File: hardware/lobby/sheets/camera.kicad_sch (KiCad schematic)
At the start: 1 part

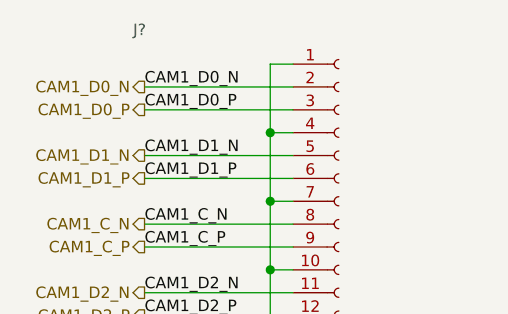
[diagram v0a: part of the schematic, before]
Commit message: start routing mezzanine
making a progress capture before trying to cram a lot of signals onto just one hirose connector...
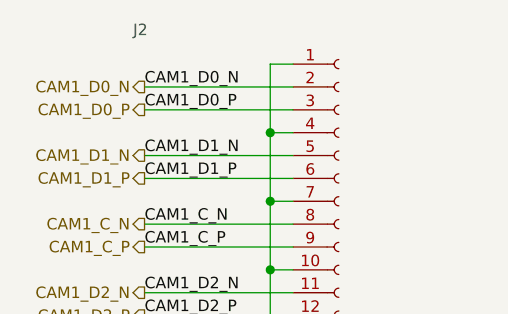
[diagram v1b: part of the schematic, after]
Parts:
- gave numbers to parts that had none: 1
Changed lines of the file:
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@@
   (symbol (lib_id "power:GND") (at 146.05 113.03 0) (unit 1)
     (in_bom yes) (on_board yes)
-    (property "Reference" "#PWR?" (id 0) (at 146.05 119.38 0)
+    (property "Reference" "#PWR0117" (id 0) (at 146.05 119.38 0)
       (effects (font (size 1.27 1.27)) hide)
     )
@@
   (symbol (lib_id "Connector:Conn_01x22_Female") (at 153.67 83.82 0) (unit 1)
     (in_bom yes) (on_board yes)
-    (property "Reference" "J?" (id 0) (at 130.81 54.61 0)
+    (property "Reference" "J2" (id 0) (at 130.81 54.61 0)
       (effects (font (size 1.27 1.27)) (justify left))
     )

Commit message: sheet refs relative, copied escalator pinout to lobby
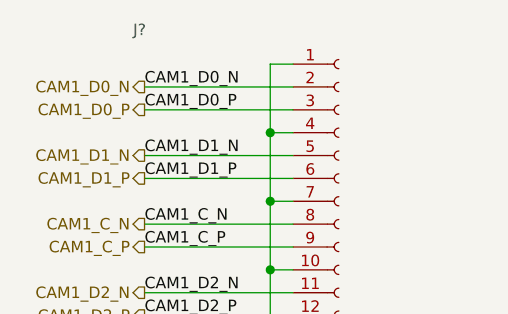
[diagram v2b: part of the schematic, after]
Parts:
- renumbered J2 to J?
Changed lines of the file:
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@@
   (symbol (lib_id "power:GND") (at 146.05 113.03 0) (unit 1)
     (in_bom yes) (on_board yes)
-    (property "Reference" "#PWR0117" (id 0) (at 146.05 119.38 0)
+    (property "Reference" "#PWR?" (id 0) (at 146.05 119.38 0)
       (effects (font (size 1.27 1.27)) hide)
     )
@@
   (symbol (lib_id "Connector:Conn_01x22_Female") (at 153.67 83.82 0) (unit 1)
     (in_bom yes) (on_board yes)
-    (property "Reference" "J2" (id 0) (at 130.81 54.61 0)
+    (property "Reference" "J?" (id 0) (at 130.81 54.61 0)
       (effects (font (size 1.27 1.27)) (justify left))
     )

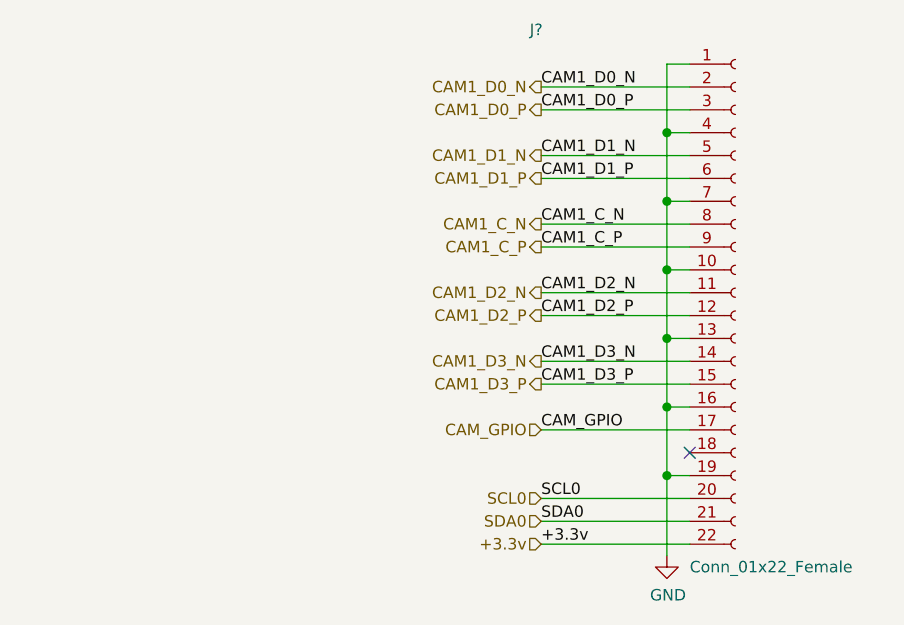
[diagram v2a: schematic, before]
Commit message: work abroad
did some light planning for the lobby board while on vacation. now ready for final placement + routing
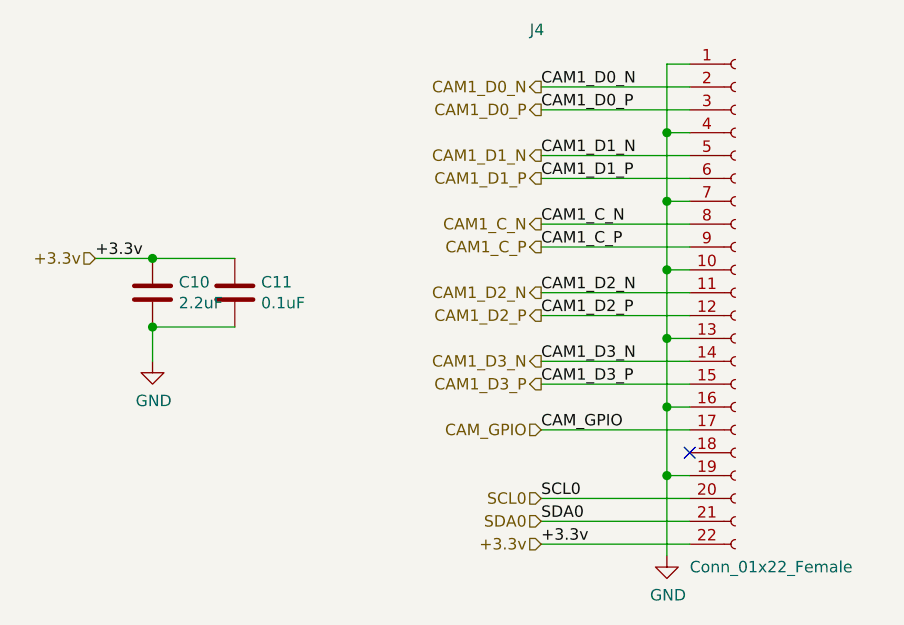
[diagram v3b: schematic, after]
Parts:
- added C10: 2.2uF, Capacitor_SMD:C_0603_1608Metric, symbol Device:C
- added C11: 0.1uF, Capacitor_SMD:C_0603_1608Metric, symbol Device:C
- gave numbers to parts that had none: 1
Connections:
- net +3.3v: now also C10.1, C11.1
- net GND: now also C10.2, C11.2
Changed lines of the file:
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@@
 (kicad_sch (version 20210406) (generator eeschema)
   (paper "A4")
+  (junction (at 88.9 80.01) (diameter 1.016) (color 0 0 0 0))
+  (junction (at 88.9 87.63) (diameter 1.016) (color 0 0 0 0))
   (junction (at 146.05 66.04) (diameter 1.016) (color 0 0 0 0))
   (junction (at 146.05 73.66) (diameter 1.016) (color 0 0 0 0))
@@
   (junction (at 146.05 104.14) (diameter 1.016) (color 0 0 0 0))
   (no_connect (at 148.59 101.6))
+  (wire (pts (xy 82.55 80.01) (xy 88.9 80.01))
+    (stroke (width 0) (type solid) (color 0 0 0 0))
+  )
+  (wire (pts (xy 88.9 80.01) (xy 98.044 80.01))
+    (stroke (width 0) (type solid) (color 0 0 0 0))
+  )
+  (wire (pts (xy 88.9 87.63) (xy 98.044 87.63))
+    (stroke (width 0) (type solid) (color 0 0 0 0))
+  )
+  (wire (pts (xy 88.9 91.44) (xy 88.9 87.63))
+    (stroke (width 0) (type solid) (color 0 0 0 0))
+  )
   (wire (pts (xy 132.08 60.96) (xy 148.59 60.96))
     (stroke (width 0) (type solid) (color 0 0 0 0))
@@
     (stroke (width 0) (type solid) (color 0 0 0 0))
   )
+  (label "+3.3v" (at 82.55 80.01 0)
+    (effects (font (size 1.27 1.27)) (justify left bottom))
+  )
   (label "CAM1_D0_N" (at 132.08 60.96 0)
     (effects (font (size 1.27 1.27)) (justify left bottom))
@@
     (effects (font (size 1.27 1.27)) (justify left bottom))
   )
+  (hierarchical_label "+3.3v" (shape input) (at 82.55 80.01 180)
+    (effects (font (size 1.27 1.27)) (justify right))
+  )
   (hierarchical_label "CAM1_D0_N" (shape output) (at 132.08 60.96 180)
     (effects (font (size 1.27 1.27)) (justify right))
@@
     (effects (font (size 1.27 1.27)) (justify right))
   )
+  (symbol (lib_id "power:GND") (at 88.9 91.44 0) (unit 1)
+    (in_bom yes) (on_board yes)
+    (property "Reference" "#PWR0101" (id 0) (at 88.9 97.79 0)
+      (effects (font (size 1.27 1.27)) hide)
+    )
+    (property "Value" "GND" (id 1) (at 89.027 95.8342 0))
+    (property "Footprint" "" (id 2) (at 88.9 91.44 0)
+      (effects (font (size 1.27 1.27)) hide)
+    )
+    (property "Datasheet" "" (id 3) (at 88.9 91.44 0)
+      (effects (font (size 1.27 1.27)) hide)
+    )
+    (pin "1")
+  )
   (symbol (lib_id "power:GND") (at 146.05 113.03 0) (unit 1)
     (in_bom yes) (on_board yes)
-    (property "Reference" "#PWR?" (id 0) (at 146.05 119.38 0)
+    (property "Reference" "#PWR0102" (id 0) (at 146.05 119.38 0)
       (effects (font (size 1.27 1.27)) hide)
     )
@@
     (pin "1")
   )
+  (symbol (lib_id "Device:C") (at 88.9 83.82 0) (unit 1)
+    (in_bom yes) (on_board yes)
+    (property "Reference" "C10" (id 0) (at 91.821 82.6516 0)
+      (effects (font (size 1.27 1.27)) (justify left))
+    )
+    (property "Value" "2.2uF" (id 1) (at 91.821 84.963 0)
+      (effects (font (size 1.27 1.27)) (justify left))
+    )
+    (property "Footprint" "Capacitor_SMD:C_0603_1608Metric" (id 2) (at 89.8652 87.63 0)
+      (effects (font (size 1.27 1.27)) hide)
+    )
+    (property "Datasheet" "https://search.murata.co.jp/Ceramy/image/img/A01X/G101/ENG/GRM21BR71A106KA73-01.pdf" (id 3) (at 88.9 83.82 0)
+      (effects (font (size 1.27 1.27)) hide)
+    )
+    (property "Field5" "490-14381-1-ND" (id 4) (at 88.9 83.82 0)
+      (effects (font (size 1.27 1.27)) hide)
+    )
+    (property "Field4" "Digikey" (id 5) (at 88.9 83.82 0)
+      (effects (font (size 1.27 1.27)) hide)
+    )
+    (property "Field6" "GRM21BR71A106KA73L" (id 6) (at 88.9 83.82 0)
+      (effects (font (size 1.27 1.27)) hide)
+    )
+    (property "Field7" "Murata" (id 7) (at 88.9 83.82 0)
+      (effects (font (size 1.27 1.27)) hide)
+    )
+    (property "Part Description" "	10uF 10% 10V Ceramic Capacitor X7R 0805 (2012 Metric)" (id 8) (at 88.9 83.82 0)
+      (effects (font (size 1.27 1.27)) hide)
+    )
+    (property "Field8" "111893011" (id 9) (at 88.9 83.82 0)
+      (effects (font (size 1.27 1.27)) hide)
+    )
+    (pin "1")
+    (pin "2")
+  )
+  (symbol (lib_id "Device:C") (at 98.044 83.82 0) (unit 1)
+    (in_bom yes) (on_board yes)
+    (property "Reference" "C11" (id 0) (at 100.965 82.6516 0)
+      (effects (font (size 1.27 1.27)) (justify left))
+    )
+    (property "Value" "0.1uF" (id 1) (at 100.965 84.963 0)
+      (effects (font (size 1.27 1.27)) (justify left))
+    )
+    (property "Footprint" "Capacitor_SMD:C_0603_1608Metric" (id 2) (at 99.0092 87.63 0)
+      (effects (font (size 1.27 1.27)) hide)
+    )
+    (property "Datasheet" "https://search.murata.co.jp/Ceramy/image/img/A01X/G101/ENG/GRM21BR71A106KA73-01.pdf" (id 3) (at 98.044 83.82 0)
+      (effects (font (size 1.27 1.27)) hide)
+    )
+    (property "Field5" "490-14381-1-ND" (id 4) (at 98.044 83.82 0)
+      (effects (font (size 1.27 1.27)) hide)
+    )
+    (property "Field4" "Digikey" (id 5) (at 98.044 83.82 0)
+      (effects (font (size 1.27 1.27)) hide)
+    )
+    (property "Field6" "GRM21BR71A106KA73L" (id 6) (at 98.044 83.82 0)
+      (effects (font (size 1.27 1.27)) hide)
+    )
+    (property "Field7" "Murata" (id 7) (at 98.044 83.82 0)
+      (effects (font (size 1.27 1.27)) hide)
+    )
+    (property "Part Description" "	10uF 10% 10V Ceramic Capacitor X7R 0805 (2012 Metric)" (id 8) (at 98.044 83.82 0)
+      (effects (font (size 1.27 1.27)) hide)
+    )
+    (property "Field8" "111893011" (id 9) (at 98.044 83.82 0)
+      (effects (font (size 1.27 1.27)) hide)
+    )
+    (pin "1")
+    (pin "2")
+  )
   (symbol (lib_id "Connector:Conn_01x22_Female") (at 153.67 83.82 0) (unit 1)
     (in_bom yes) (on_board yes)
-    (property "Reference" "J?" (id 0) (at 130.81 54.61 0)
-      (effects (font (size 1.27 1.27)) (justify left))
-    )
+    (property "Reference" "J4" (id 0) (at 130.81 54.61 0)
+      (effects (font (size 1.27 1.27)) (justify left))
+    )

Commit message: update lobby
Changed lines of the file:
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@@
   (symbol (lib_id "power:GND") (at 88.9 91.44 0) (unit 1)
     (in_bom yes) (on_board yes)
-    (property "Reference" "#PWR0101" (id 0) (at 88.9 97.79 0)
+    (property "Reference" "#PWR0100" (id 0) (at 88.9 97.79 0)
       (effects (font (size 1.27 1.27)) hide)
     )
@@
   (symbol (lib_id "power:GND") (at 146.05 113.03 0) (unit 1)
     (in_bom yes) (on_board yes)
-    (property "Reference" "#PWR0102" (id 0) (at 146.05 119.38 0)
+    (property "Reference" "#PWR0101" (id 0) (at 146.05 119.38 0)
       (effects (font (size 1.27 1.27)) hide)
     )
@@
       (effects (font (size 1.27 1.27)) hide)
     )
-    (property "Datasheet" "https://search.murata.co.jp/Ceramy/image/img/A01X/G101/ENG/GRM21BR71A106KA73-01.pdf" (id 3) (at 88.9 83.82 0)
+    (property "Datasheet" "~" (id 3) (at 88.9 83.82 0)
       (effects (font (size 1.27 1.27)) hide)
     )
@@
       (effects (font (size 1.27 1.27)) hide)
     )
-    (property "Datasheet" "https://search.murata.co.jp/Ceramy/image/img/A01X/G101/ENG/GRM21BR71A106KA73-01.pdf" (id 3) (at 98.044 83.82 0)
+    (property "Datasheet" "~" (id 3) (at 98.044 83.82 0)
       (effects (font (size 1.27 1.27)) hide)
     )
@@
       (effects (font (size 1.27 1.27)) hide)
     )
-    (property "Datasheet" "https://www.hirose.com/product/document?clcode=&productname=&series=FH12&documenttype=Catalog&lang=en&documentid=D31648_en" (id 3) (at 153.67 83.82 0)
+    (property "Datasheet" "~" (id 3) (at 153.67 83.82 0)
       (effects (font (size 1.27 1.27)) hide)
     )

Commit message: update camera connector footprint
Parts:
- J4: footprint Connector_FFC-FPC:Hirose_FH12-22S-0.5SH_1x22-1MP_P0.50mm_Horizontal -> cm4crypto:SFV22R-2STE1HLF
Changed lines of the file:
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@@
       (effects (font (size 1.27 1.27)) (justify left))
     )
-    (property "Footprint" "Connector_FFC-FPC:Hirose_FH12-22S-0.5SH_1x22-1MP_P0.50mm_Horizontal" (id 2) (at 153.67 83.82 0)
+    (property "Footprint" "cm4crypto:SFV22R-2STE1HLF" (id 2) (at 153.67 83.82 0)
       (effects (font (size 1.27 1.27)) hide)
     )
